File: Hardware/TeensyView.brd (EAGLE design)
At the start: 160 x 100 mm, 9 parts

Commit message: Proto 1 design complete
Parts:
- removed J3: (no value), SparkFun-Connectors:1X01
- added C1, C2, C3, C4: 1.0uF, SparkFun-Capacitors:0402
- added C5: 2.2uF, SparkFun-Capacitors:0805
- added C6: 4.7UF, SparkFun-Capacitors:1206
- added JP1, JP2, JP3: JUMPER-SMT_3_1-NC_TRACE_SILK, SparkFun-Jumpers:SMT-JUMPER_3_1-NC_TRACE_SILK
- added OLED1: OLED128X64SIDEREAR-MOUNT, TeensyViewDev:OLED-UG-2832TSWGG01-REAR
- added R1: 330k, SparkFun-Resistors:0603
- J1, J2: value (none) -> DNP; device SparkFun-Connectors:1X14 -> SparkFun-Connectors:1X14_NO_SILK
- moved FD2 50.8 mm to (5.08, 15.0), flipped to the bottom
- moved LOGO1 46.2 mm to (9.92, 11.0), flipped to the bottom
- moved LOGO3 42.9 mm to (13.0, 1.98)
- moved J2 35.9 mm to (1.27, 1.27)
- moved J1 35.9 mm to (34.3, 16.5)
- moved FD1 25.3 mm to (34.3, 3.41), flipped to the bottom
- moved LOGO2 22.8 mm to (33.1, 10.3)
- moved FRAME1 16.3 mm to (-14.0, -24.1)
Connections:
- new net !CS: JP1.2, OLED1.8
- new net !RESET: J1.8, OLED1.9
- new net D/!C: J1.7, OLED1.10
- new net N$1: J1.12, JP1.3
- new net N$10: J2.1, JP3.3
- new net N$11: J2.7, JP3.1
- new net N$12: J1.13, JP2.3
- new net N$13: J2.6, JP2.1
- new net N$2: J1.11, JP1.1
- new net N$3: C4.2, OLED1.4
- new net N$4: C4.1, OLED1.3
- new net N$5: C3.2, OLED1.2
- new net N$6: C3.1, OLED1.1
- new net N$7: OLED1.13, R1.2
- new net N$8: C6.1, OLED1.14
- new net N$9: C5.1, OLED1.15
- new net SCLK: JP3.2, OLED1.11
- new net SDIN: JP2.2, OLED1.12
- new net VCC: C1.1, C2.1, J2.12, OLED1.5, OLED1.7
- net GND: now also C1.2, C2.2, C5.2, C6.2, J1.1, OLED1.6, R1.1; no longer J3.1
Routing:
- net !CS: track 0.00 -> 31.8 mm, vias 0 -> 1
- net !RESET: track 0.00 -> 30.9 mm, vias 0 -> 1
- net D/!C: track 0.00 -> 28.9 mm, vias 0 -> 1
- net SCLK: track 0.00 -> 26.3 mm, vias 0 -> 1
- net SDIN: track 0.00 -> 20.6 mm, vias 0 -> 1
- net VCC: track 0.00 -> 17.9 mm
- net N$7: track 0.00 -> 13.9 mm, vias 0 -> 2
- net N$13: track 0.00 -> 11.3 mm, vias 0 -> 1
- net N$10: track 0.00 -> 11.2 mm
- net N$12: track 0.00 -> 10.2 mm
- net N$11: track 0.00 -> 9.47 mm
- net GND: track 0.00 -> 5.95 mm, vias 1 -> 11
- net N$3: track 0.00 -> 5.32 mm
- net N$5: track 0.00 -> 5.31 mm
- net N$1: track 0.00 -> 5.00 mm
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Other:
- board size 160 x 100 mm -> 35.6 x 17.8 mm
- board text added: "!CS"
- board text added: "10"
- board text added: "11"
- board text added: "13"
- board text added: "9"
- board text added: "A4"
- board text added: "A5"
- board text added: "DATA"
- board text added: "Measurements in inches"
- board text added: "SCLK"
- board text added: "TeensyView"

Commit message: Post review fixes
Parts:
- added JP4: JUMPER-SMT_3_2-NC_TRACE_SILK, SparkFun-Jumpers:SMT-JUMPER_3_2-NC_TRACE_SILK
- added R2, R3, R4: 4.7k, SparkFun-Resistors:0603
- moved LOGO3 8.59 mm to (16.0, 10.0)
- moved LOGO1 8.12 mm to (9.29, 2.86)
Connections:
- new net A4PU: JP4.3, R2.2
- new net A5PU: JP4.1, R3.2
- net !CS: now also R4.1
- net N$11: now also R3.1
- net N$13: now also R2.1
- net VCC: now also JP4.2, R4.2
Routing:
- net VCC: track 17.9 -> 32.0 mm, vias 0 -> 1
- net !CS: track 31.8 -> 43.3 mm, vias 1 -> 2
- net A4PU: track 0.00 -> 7.02 mm, vias 0 -> 1
- net N$11: track 9.47 -> 15.1 mm
- net A5PU: track 0.00 -> 3.66 mm, vias 0 -> 1
- net N$13: track 11.3 -> 13.0 mm
- net GND: vias 11 -> 12
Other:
- board text added: "PULL ENB"

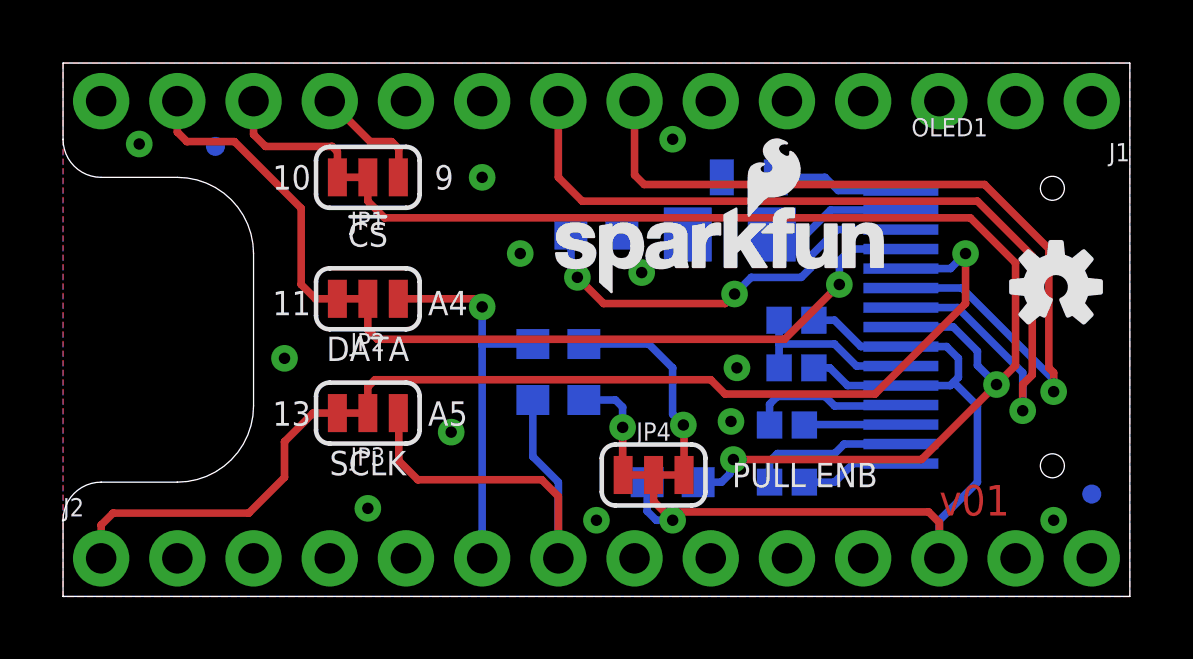
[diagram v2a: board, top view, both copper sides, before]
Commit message: Resized dimension, moved 1 via and added a couple more
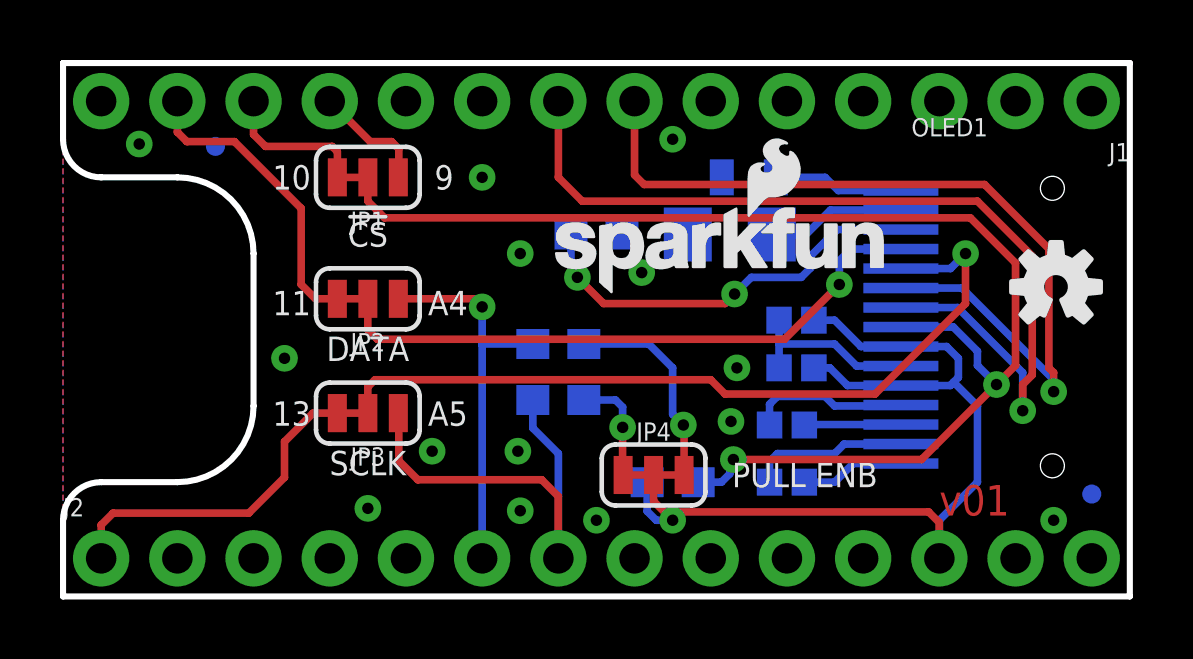
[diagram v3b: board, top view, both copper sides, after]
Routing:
- net GND: vias 12 -> 14
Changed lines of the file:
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@@
 <setting verticaltext="up"/>
 </settings>
-<grid distance="0.05" unitdist="inch" unit="inch" style="lines" multiple="1" display="yes" altdistance="0.0015625" altunitdist="inch" altunit="inch"/>
+<grid distance="0.05" unitdist="inch" unit="inch" style="lines" multiple="1" display="yes" altdistance="0.0125" altunitdist="inch" altunit="inch"/>
 <layers>
-<layer number="1" name="Top" color="4" fill="1" visible="no" active="yes"/>
+<layer number="1" name="Top" color="4" fill="1" visible="yes" active="yes"/>
 <layer number="2" name="Route2" color="1" fill="3" visible="no" active="no"/>
 <layer number="3" name="Route3" color="4" fill="3" visible="no" active="no"/>
@@
 <layer number="19" name="Unrouted" color="6" fill="1" visible="yes" active="yes"/>
 <layer number="20" name="Dimension" color="15" fill="1" visible="yes" active="yes"/>
-<layer number="21" name="tPlace" color="16" fill="1" visible="no" active="yes"/>
+<layer number="21" name="tPlace" color="16" fill="1" visible="yes" active="yes"/>
 <layer number="22" name="bPlace" color="14" fill="1" visible="yes" active="yes"/>
 <layer number="23" name="tOrigins" color="15" fill="1" visible="no" active="yes"/>
-<layer number="24" name="bOrigins" color="15" fill="1" visible="yes" active="yes"/>
+<layer number="24" name="bOrigins" color="15" fill="1" visible="no" active="yes"/>
 <layer number="25" name="tNames" color="7" fill="1" visible="no" active="yes"/>
 <layer number="26" name="bNames" color="7" fill="1" visible="no" active="yes"/>
@@
 <board>
 <plain>
-<wire x1="0" y1="0" x2="35.56" y2="0" width="0" layer="20"/>
-<wire x1="35.56" y1="0" x2="35.56" y2="17.78" width="0" layer="20"/>
-<wire x1="35.56" y1="17.78" x2="0" y2="17.78" width="0" layer="20"/>
-<wire x1="0" y1="17.78" x2="0" y2="15.24" width="0" layer="20"/>
-<wire x1="0" y1="15.24" x2="1.27" y2="13.97" width="0" layer="20" curve="90"/>
-<wire x1="1.27" y1="13.97" x2="3.81" y2="13.97" width="0" layer="20"/>
-<wire x1="3.81" y1="13.97" x2="6.35" y2="11.43" width="0" layer="20" curve="-90"/>
-<wire x1="6.35" y1="11.43" x2="6.35" y2="6.35" width="0" layer="20"/>
-<wire x1="6.35" y1="6.35" x2="3.81" y2="3.81" width="0" layer="20" curve="-90"/>
-<wire x1="3.81" y1="3.81" x2="1.27" y2="3.81" width="0" layer="20"/>
-<wire x1="1.27" y1="3.81" x2="0" y2="2.54" width="0" layer="20" curve="90"/>
-<wire x1="0" y1="2.54" x2="0" y2="0" width="0" layer="20"/>
-<wire x1="0" y1="0" x2="35.56" y2="0" width="0.254" layer="51"/>
-<wire x1="35.56" y1="0" x2="35.56" y2="17.78" width="0.254" layer="51"/>
-<wire x1="35.56" y1="17.78" x2="0" y2="17.78" width="0.254" layer="51"/>
+<wire x1="0" y1="0" x2="35.56" y2="0" width="0.2032" layer="20"/>
+<wire x1="35.56" y1="0" x2="35.56" y2="17.78" width="0.2032" layer="20"/>
+<wire x1="35.56" y1="17.78" x2="0" y2="17.78" width="0.2032" layer="20"/>
+<wire x1="0" y1="17.78" x2="0" y2="15.24" width="0.2032" layer="20"/>
+<wire x1="0" y1="15.24" x2="1.27" y2="13.97" width="0.2032" layer="20" curve="90"/>
+<wire x1="1.27" y1="13.97" x2="3.81" y2="13.97" width="0.2032" layer="20"/>
+<wire x1="3.81" y1="13.97" x2="6.35" y2="11.43" width="0.2032" layer="20" curve="-90"/>
+<wire x1="6.35" y1="11.43" x2="6.35" y2="6.35" width="0.2032" layer="20"/>
+<wire x1="6.35" y1="6.35" x2="3.81" y2="3.81" width="0.2032" layer="20" curve="-90"/>
+<wire x1="3.81" y1="3.81" x2="1.27" y2="3.81" width="0.2032" layer="20"/>
+<wire x1="1.27" y1="3.81" x2="0" y2="2.54" width="0.2032" layer="20" curve="90"/>
+<wire x1="0" y1="2.54" x2="0" y2="0" width="0.2032" layer="20"/>
 <text x="29.21" y="2.69875" size="1.016" layer="1" font="vector" ratio="25">v01</text>
 <text x="17.78" y="-24.13" size="1.778" layer="51" font="vector">Marshall Taylor</text>
-<wire x1="0" y1="0" x2="0" y2="2.54" width="0.254" layer="51"/>
-<wire x1="0" y1="2.54" x2="1.27" y2="3.81" width="0.254" layer="51" curve="-90"/>
-<wire x1="1.27" y1="3.81" x2="3.81" y2="3.81" width="0.254" layer="51"/>
-<wire x1="3.81" y1="3.81" x2="6.35" y2="6.35" width="0.254" layer="51" curve="90"/>
-<wire x1="6.35" y1="6.35" x2="6.35" y2="11.43" width="0.254" layer="51"/>
-<wire x1="6.35" y1="11.43" x2="3.81" y2="13.97" width="0.254" layer="51" curve="90"/>
-<wire x1="3.81" y1="13.97" x2="1.27" y2="13.97" width="0.254" layer="51"/>
-<wire x1="1.27" y1="13.97" x2="0" y2="15.24" width="0.254" layer="51" curve="-90"/>
-<wire x1="0" y1="15.24" x2="0" y2="17.78" width="0.254" layer="51"/>
 <text x="10.16" y="4.445" size="0.8128" layer="21" font="vector" ratio="15" align="center">SCLK</text>
 <text x="7.62" y="6.096" size="0.8128" layer="21" font="vector" ratio="15" align="center">13</text>
@@
 <via x="17.78" y="2.54" extent="1-16" drill="0.381"/>
 <via x="22.463125" y="7.62" extent="1-16" drill="0.381"/>
-<via x="12.938125" y="5.476875" extent="1-16" drill="0.381"/>
+<via x="12.303125" y="4.841875" extent="1-16" drill="0.381"/>
 <via x="22.2646875" y="5.8340625" extent="1-16" drill="0.381"/>
+<via x="15.24" y="2.8575" extent="1-16" drill="0.381"/>
+<via x="15.160625" y="4.841875" extent="1-16" drill="0.381"/>
 </signal>
 <signal name="N$3">
@@
 <wire x1="11.191875" y1="6.096" x2="11.176" y2="6.111875" width="0.254" layer="1"/>
 <contactref element="R3" pad="1"/>
-<wire x1="15.66" y1="6.5484375" x2="15.66" y2="4.66" width="0.254" layer="16"/>
-<wire x1="15.66" y1="4.66" x2="16.51" y2="3.81" width="0.254" layer="16"/>
-<wire x1="16.51" y1="3.81" x2="16.51" y2="1.27" width="0.254" layer="16"/>
+<wire x1="15.66" y1="6.5484375" x2="15.66" y2="5.6125" width="0.254" layer="16"/>
+<wire x1="15.66" y1="5.6125" x2="16.51" y2="4.7625" width="0.254" layer="16"/>
+<wire x1="16.51" y1="4.7625" x2="16.51" y2="1.27" width="0.254" layer="16"/>
 </signal>
 <signal name="N$10">

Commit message: Going for proto 2
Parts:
- removed R2, R3: 4.7k, SparkFun-Resistors:0603
- added JP5: JUMPER-SMT_3_1-NC_TRACE_SILK, SparkFun-Jumpers:SMT-JUMPER_3_1-NC_TRACE_SILK
- JP4: value JUMPER-SMT_3_2-NC_TRACE_SILK -> JUMPER-SMT_3_1-NC_TRACE_SILK; device SparkFun-Jumpers:SMT-JUMPER_3_2-NC_TRACE_SILK -> SparkFun-Jumpers:SMT-JUMPER_3_1-NC_TRACE_SILK
- moved LOGO3 14.6 mm to (28.7, 2.79), turned to 90 degrees
- moved JP1 6.35 mm to (14.0, 8.89), turned to 90 degrees
- moved JP4 5.79 mm to (16.5, 8.89), turned to 90 degrees
- moved JP3 3.05 mm to (8.89, 8.89), turned to 90 degrees
- moved JP2 1.64 mm to (11.4, 8.89), turned to 90 degrees
- moved LOGO2 1.15 mm to (33.8, 11.2), turned to 90 degrees
- turned R4 to 180 degrees
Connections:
- removed net A4PU: JP4.3, R2.2
- removed net A5PU: JP4.1, R3.2
- new net N$14: J2.3, JP4.3
- new net N$15: J1.4, JP4.1
- new net N$16: J1.7, JP5.3
- new net N$17: J2.9, JP5.1
- net !RESET: now also JP4.2; no longer J1.8
- net D/!C: now also JP5.2; no longer J1.7
- net N$11: now also J2.2; no longer J2.7, R3.1
- net N$13: now also J1.9; no longer J2.6, R2.1
- net N$2: now also J2.8; no longer J1.11
- net VCC: no longer JP4.2
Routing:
- net N$15: track 0.00 -> 24.1 mm, vias 0 -> 2
- net N$14: track 0.00 -> 20.1 mm, vias 0 -> 1
- net N$17: track 0.00 -> 16.2 mm, vias 0 -> 1
- net !CS: track 43.3 -> 27.8 mm, vias 2 -> 3
- net N$16: track 0.00 -> 14.1 mm
- net A4PU: track 7.02 -> 0.00 mm, vias 1 -> 0
- net !RESET: track 30.9 -> 24.2 mm, vias 1 -> 3
- net N$2: track 3.92 -> 10.2 mm, vias 0 -> 1
- net N$11: track 15.1 -> 9.08 mm
- net N$1: track 5.00 -> 10.7 mm
- net D/!C: track 28.9 -> 23.2 mm
- net N$10: track 11.2 -> 16.3 mm, vias 0 -> 1
- net VCC: track 32.0 -> 27.0 mm, vias 1 -> 0
- net SCLK: track 26.4 -> 31.3 mm
- net A5PU: track 3.66 -> 0.00 mm, vias 1 -> 0
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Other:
- board text added: "!RST"
- board text added: "0"
- board text added: "12"
- board text added: "14"
- board text added: "15"
- board text added: "2"
- board text added: "20"
- board text added: "21"
- board text added: "3V"
- board text added: "5"
- board text added: "7"
- board text added: "Alternate"
- board text added: "D/!C"
- board text added: "G"
- board text added: "GND"
- board text added: "ROUTE OUT"
- board text added: "Standard"
- board text added: "v02"
- board text removed: "9"
- board text removed: "A4"
- board text removed: "A5"
- board text removed: "PULL ENB"
- board text removed: "v01"

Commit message: Applied Proto 2 review action items
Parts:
- R1: value 330k -> 820k
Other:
- board text added: "1"
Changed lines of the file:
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@@
 <setting verticaltext="up"/>
 </settings>
-<grid distance="0.05" unitdist="inch" unit="inch" style="lines" multiple="1" display="yes" altdistance="0.005" altunitdist="inch" altunit="inch"/>
+<grid distance="0.05" unitdist="inch" unit="inch" style="lines" multiple="1" display="yes" altdistance="0.0025" altunitdist="inch" altunit="inch"/>
 <layers>
-<layer number="1" name="Top" color="4" fill="1" visible="yes" active="yes"/>
+<layer number="1" name="Top" color="4" fill="1" visible="no" active="yes"/>
 <layer number="2" name="Route2" color="1" fill="3" visible="no" active="no"/>
 <layer number="3" name="Route3" color="4" fill="3" visible="no" active="no"/>
@@
 <layer number="19" name="Unrouted" color="6" fill="1" visible="yes" active="yes"/>
 <layer number="20" name="Dimension" color="15" fill="1" visible="yes" active="yes"/>
-<layer number="21" name="tPlace" color="16" fill="1" visible="yes" active="yes"/>
+<layer number="21" name="tPlace" color="16" fill="1" visible="no" active="yes"/>
 <layer number="22" name="bPlace" color="14" fill="1" visible="yes" active="yes"/>
-<layer number="23" name="tOrigins" color="15" fill="1" visible="yes" active="yes"/>
+<layer number="23" name="tOrigins" color="15" fill="1" visible="no" active="yes"/>
 <layer number="24" name="bOrigins" color="15" fill="1" visible="yes" active="yes"/>
 <layer number="25" name="tNames" color="7" fill="1" visible="no" active="yes"/>
@@
 <layer number="27" name="tValues" color="7" fill="1" visible="no" active="yes"/>
 <layer number="28" name="bValues" color="7" fill="1" visible="no" active="yes"/>
-<layer number="29" name="tStop" color="7" fill="3" visible="no" active="yes"/>
-<layer number="30" name="bStop" color="7" fill="6" visible="no" active="yes"/>
-<layer number="31" name="tCream" color="7" fill="4" visible="no" active="yes"/>
-<layer number="32" name="bCream" color="7" fill="5" visible="no" active="yes"/>
+<layer number="29" name="tStop" color="7" fill="3" visible="yes" active="yes"/>
+<layer number="30" name="bStop" color="7" fill="6" visible="yes" active="yes"/>
+<layer number="31" name="tCream" color="7" fill="4" visible="yes" active="yes"/>
+<layer number="32" name="bCream" color="7" fill="5" visible="yes" active="yes"/>
 <layer number="33" name="tFinish" color="6" fill="3" visible="no" active="yes"/>
 <layer number="34" name="bFinish" color="6" fill="6" visible="no" active="yes"/>
@@
 <text x="14.478" y="6.35" size="0.8128" layer="21" font="vector" ratio="15" rot="R90" align="center">20</text>
 <text x="19.558" y="6.35" size="0.8128" layer="21" font="vector" ratio="15" rot="R90" align="center">21</text>
-<text x="21.05025" y="12.09675" size="0.8128" layer="21" font="vector" ratio="15" rot="R90" align="center">Standard</text>
-<text x="21.05025" y="5.87375" size="0.8128" layer="21" font="vector" ratio="15" rot="R90" align="center">Alternate</text>
+<text x="13.97" y="13.081" size="0.8128" layer="21" font="vector" ratio="15" rot="R180" align="center">Standard</text>
+<text x="13.97" y="3.429" size="0.8128" layer="21" font="vector" ratio="15" rot="R180" align="center">Alternate</text>
 <wire x1="7.5565" y1="8.89" x2="7.8105" y2="8.89" width="0.2032" layer="21"/>
 <wire x1="6.7945" y1="8.89" x2="7.0485" y2="8.89" width="0.2032" layer="21"/>
@@
 <vertex x="5.36455625" y="2.086278125"/>
 </polygon>
-<text x="1.27" y="14.9225" size="0.8128" layer="21" font="vector" ratio="15" rot="R180" align="center">12</text>
-<text x="29.21" y="14.6685" size="0.8128" layer="21" font="vector" ratio="15" align="center">0</text>
-<text x="1.7145" y="3.048" size="0.8128" layer="21" font="vector" ratio="15" rot="R180" align="center">13</text>
+<text x="1.397" y="14.9225" size="0.8128" layer="21" font="vector" ratio="15" rot="R180" align="center">12</text>
+<text x="29.2735" y="14.9225" size="0.8128" layer="21" font="vector" ratio="15" align="center">0</text>
+<text x="1.397" y="3.048" size="0.8128" layer="21" font="vector" ratio="15" rot="R180" align="center">13</text>
 <text x="34.163" y="14.6685" size="0.8128" layer="21" font="vector" ratio="15" rot="R180" align="center">GND</text>
 <text x="29.21" y="3.048" size="0.8128" layer="21" font="vector" ratio="15" rot="R180" align="center">3V</text>
@@
 <vertex x="35.27544375" y="17.326278125"/>
 </polygon>
-<text x="1.27" y="14.9225" size="0.8128" layer="22" font="vector" ratio="15" rot="MR180" align="center">12</text>
+<text x="1.397" y="14.9225" size="0.8128" layer="22" font="vector" ratio="15" rot="MR180" align="center">12</text>
 <text x="34.7345" y="14.76375" size="0.8128" layer="22" font="vector" ratio="15" rot="MR0" align="center">G</text>
-<text x="1.27" y="3.048" size="0.8128" layer="22" font="vector" ratio="15" rot="MR180" align="center">13</text>
+<text x="1.397" y="3.048" size="0.8128" layer="22" font="vector" ratio="15" rot="MR180" align="center">13</text>
 <text x="30.353" y="2.7305" size="0.8128" layer="22" font="vector" ratio="15" rot="MR180" align="center">3V</text>
 <text x="1.27" y="5.08" size="1.016" layer="20" font="vector" ratio="15" rot="R60">ROUTE OUT</text>
+<text x="30.099" y="13.5255" size="0.8128" layer="22" font="vector" ratio="15" rot="MR0" align="center">15</text>
+<text x="29.6545" y="4.445" size="0.8128" layer="22" font="vector" ratio="15" rot="MR0" align="center">1</text>
 </plain>
 <attributes>
@@
 <attribute name="PROD_ID" value="CAP-10300" x="22.225" y="12.065" size="1.778" layer="28" rot="MR0" display="off"/>
 </element>
-<element name="R1" library="SparkFun-Resistors" package="0603" value="330k" x="17.78" y="12.065" rot="MR0">
-<attribute name="PROD_ID" value="RES-08968" x="17.78" y="12.065" size="1.778" layer="28" font="vector" ratio="15" rot="MR0" display="off"/>
+<element name="R1" library="SparkFun-Resistors" package="0603" value="820k" x="17.78" y="12.065" rot="MR0">
+<attribute name="PROD_ID" value="RES-13247" x="17.78" y="12.065" size="1.778" layer="28" font="vector" ratio="15" rot="MR0" display="off"/>
 </element>
 <element name="JP1" library="SparkFun-Jumpers" package="SMT-JUMPER_3_1-NC_TRACE_SILK" value="JUMPER-SMT_3_1-NC_TRACE_SILK" x="13.97" y="8.89" rot="R90"/>
